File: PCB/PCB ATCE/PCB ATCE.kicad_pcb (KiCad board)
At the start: 2 copper layers, 27 parts, among them J1 USB_OTG, J2 Conn_Coaxial, SW1 SW_Push, SW2 SW_Push, Y1 16MHz

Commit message: PCB
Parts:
- added REF**: MountingHole_3.2mm_M3, MountingHole:MountingHole_3.2mm_M3, F.Cu at (114.5, 106.5)
- added REF**: MountingHole_3.2mm_M3, MountingHole:MountingHole_3.2mm_M3, F.Cu at (158.5, 79.5)
- added TP1: TestPoint, TestPoint:TestPoint_Keystone_5000-5004_Miniature, F.Cu at (138.5, 79.8)
- moved J2 46.6 mm to (154.5, 90.0), turned to 180 degrees
- moved C5 36.6 mm to (126.4, 104.0)
- moved C1 35.4 mm to (143.5, 103.0), turned to 90 degrees
- moved J1 35.2 mm to (118.6, 85.6)
- moved U1 33.3 mm to (138.3, 89.5)
- moved SW1 33.3 mm to (132.5, 101.9), turned to 90 degrees
- moved C7 33.1 mm to (147.5, 93.9), turned to -90 degrees
- moved C2 32.3 mm to (140.0, 103.0), turned to 90 degrees
- moved C3 30.0 mm to (147.5, 103.0), turned to -90 degrees
- moved TP3 28.3 mm to (120.0, 107.0)
- moved TP2 27.8 mm to (129.0, 96.5)
- moved BB833 27.4 mm to (143.5, 106.0), turned to 180 degrees
- moved R1 26.4 mm to (126.5, 92.0), turned to 90 degrees
- moved C6 24.8 mm to (143.5, 81.0), turned to 180 degrees
- moved SW2 24.7 mm to (151.9, 83.5)
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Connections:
- net Net-(J1-D+) renamed /D1+
- net Net-(J1-D-) renamed /D1-
- net Net-(U1-D+) renamed /D2+
- net Net-(U1-D-) renamed /D2-
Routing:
- net +5V: track 0.00 -> 80.0 mm
- net Net-(U2--): track 0.00 -> 34.0 mm
- net GND: track 0.00 -> 32.2 mm, vias 0 -> 23
- net Net-(J1-VBUS): track 0.00 -> 24.1 mm
- net Net-(U2-+): track 0.00 -> 18.4 mm
- net Net-(U1-XTAL2): track 0.00 -> 17.2 mm
- net Net-(U1-(OC0A/OC1C/~{RTS}/PCINT7)PB7): track 0.00 -> 13.7 mm
- net /D2-: track 0.00 -> 13.3 mm
- net Net-(BB833-K): track 0.00 -> 13.2 mm
- net /D2+: track 0.00 -> 12.5 mm
- net Net-(J2-In): track 0.00 -> 11.3 mm
- net Net-(U1-XTAL1): track 0.00 -> 11.0 mm
- net /D1+: track 0.00 -> 9.94 mm
- net /D1-: track 0.00 -> 9.86 mm
- net Net-(U1-(~{HWB})PE2): track 0.00 -> 5.33 mm
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- added copper zone on B.Cu, net GND
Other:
- board outline added: 49 x 32 mm

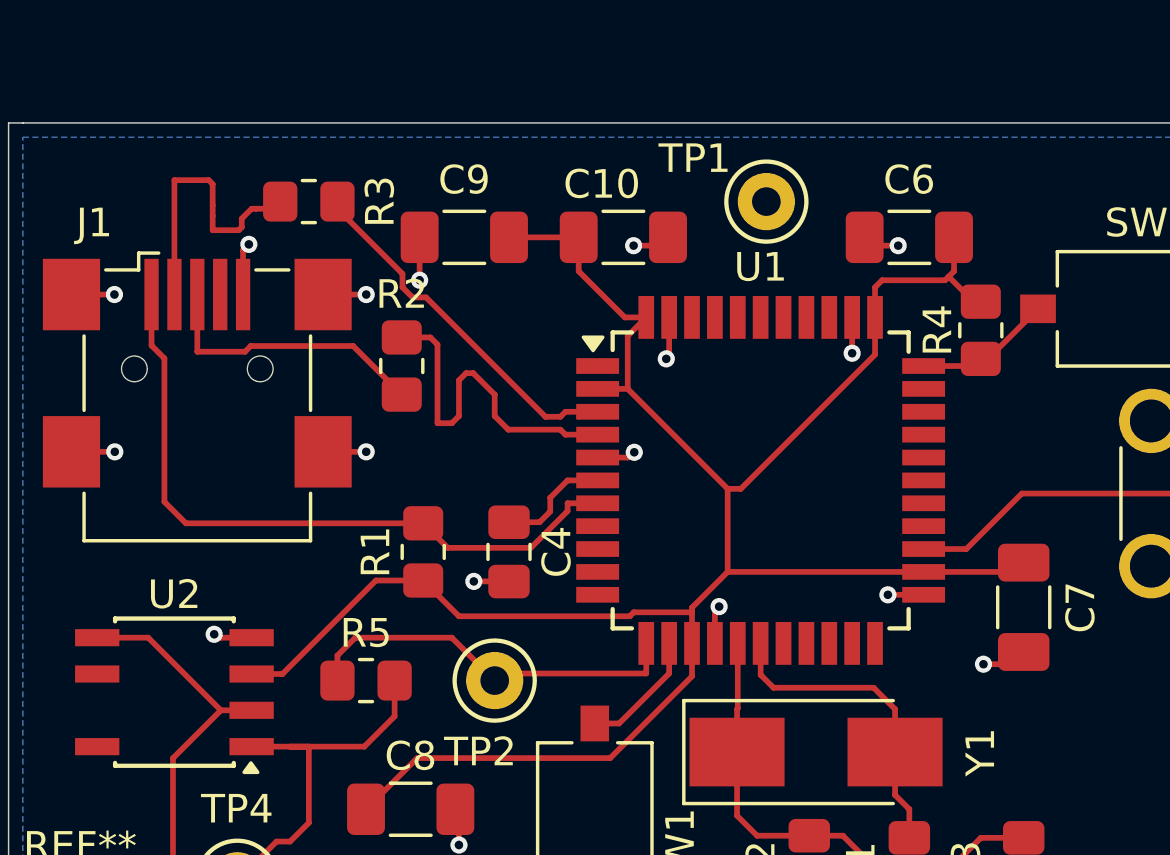
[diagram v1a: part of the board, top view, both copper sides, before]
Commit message: j'ai enlever les 90 degres
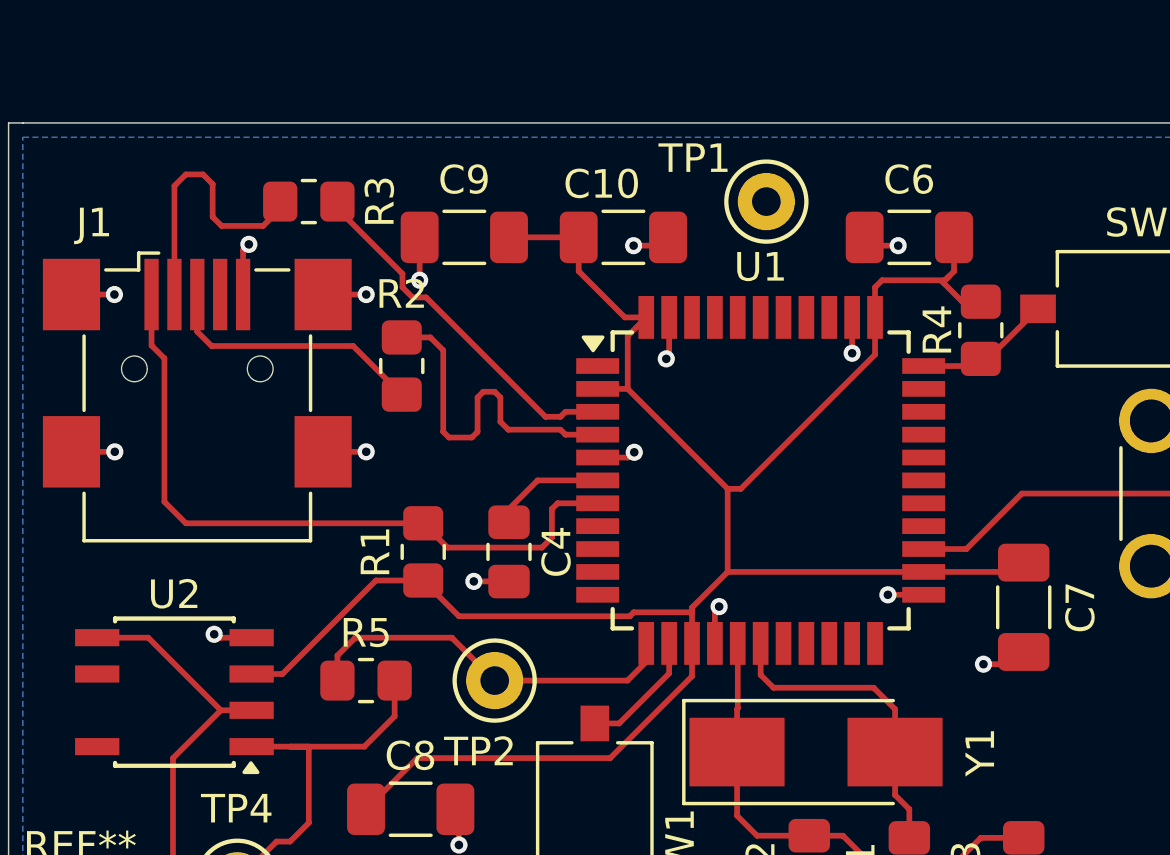
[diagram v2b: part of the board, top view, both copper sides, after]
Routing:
- net /D1+: track 9.94 -> 9.36 mm
- net /D1-: track 9.86 -> 9.33 mm

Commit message: deplace port usb
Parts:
- moved R3 3.60 mm to (125.8, 81.2), turned to -90 degrees
- moved J1 3.60 mm to (118.6, 82.0)
- moved C9 1.31 mm to (129.2, 81.4), turned to -90 degrees
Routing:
- net /D1-: track 9.33 -> 14.8 mm
- net /D1+: track 9.36 -> 14.1 mm
- net Net-(J1-VBUS): track 24.5 -> 27.8 mm
- net /D2-: track 13.3 -> 10.1 mm
- net /D2+: track 12.5 -> 9.28 mm
- net +5V: track 80.4 -> 81.7 mm

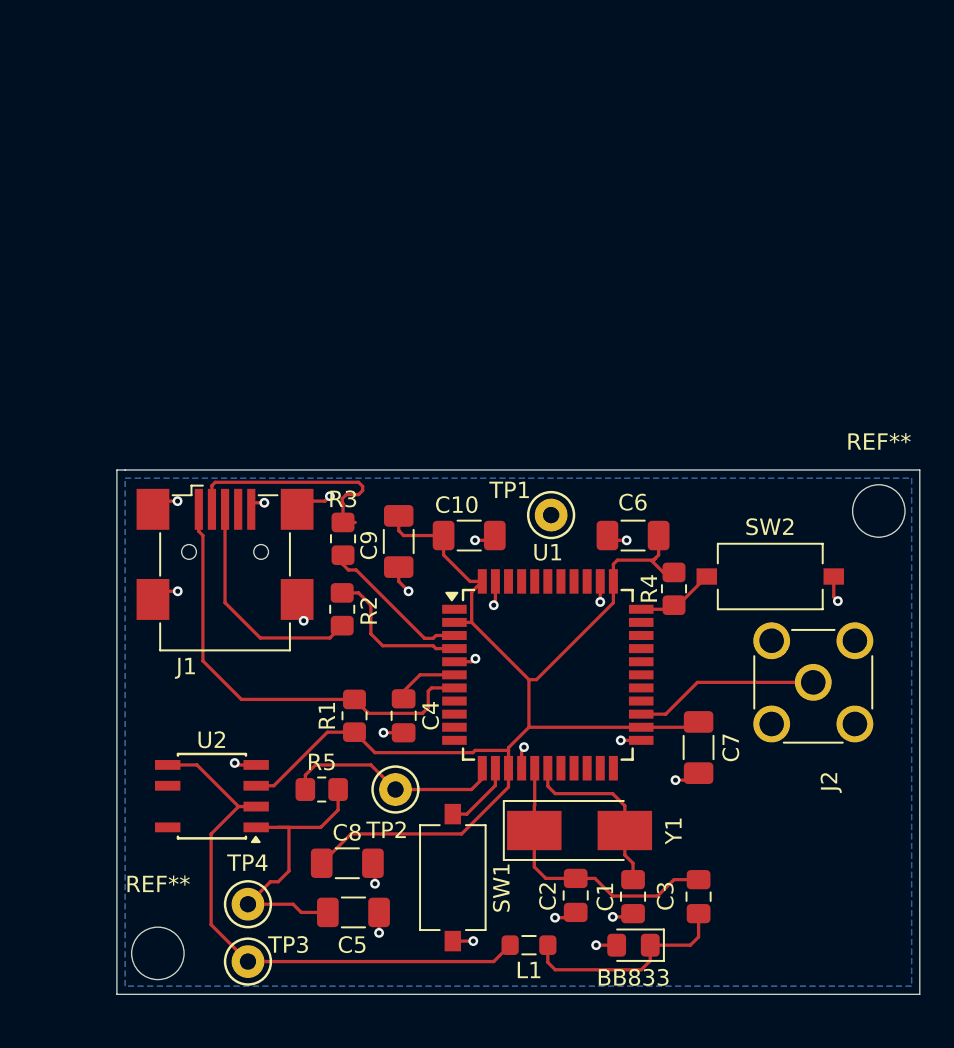
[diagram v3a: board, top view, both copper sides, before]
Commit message: PCB : retouche port usb et coax
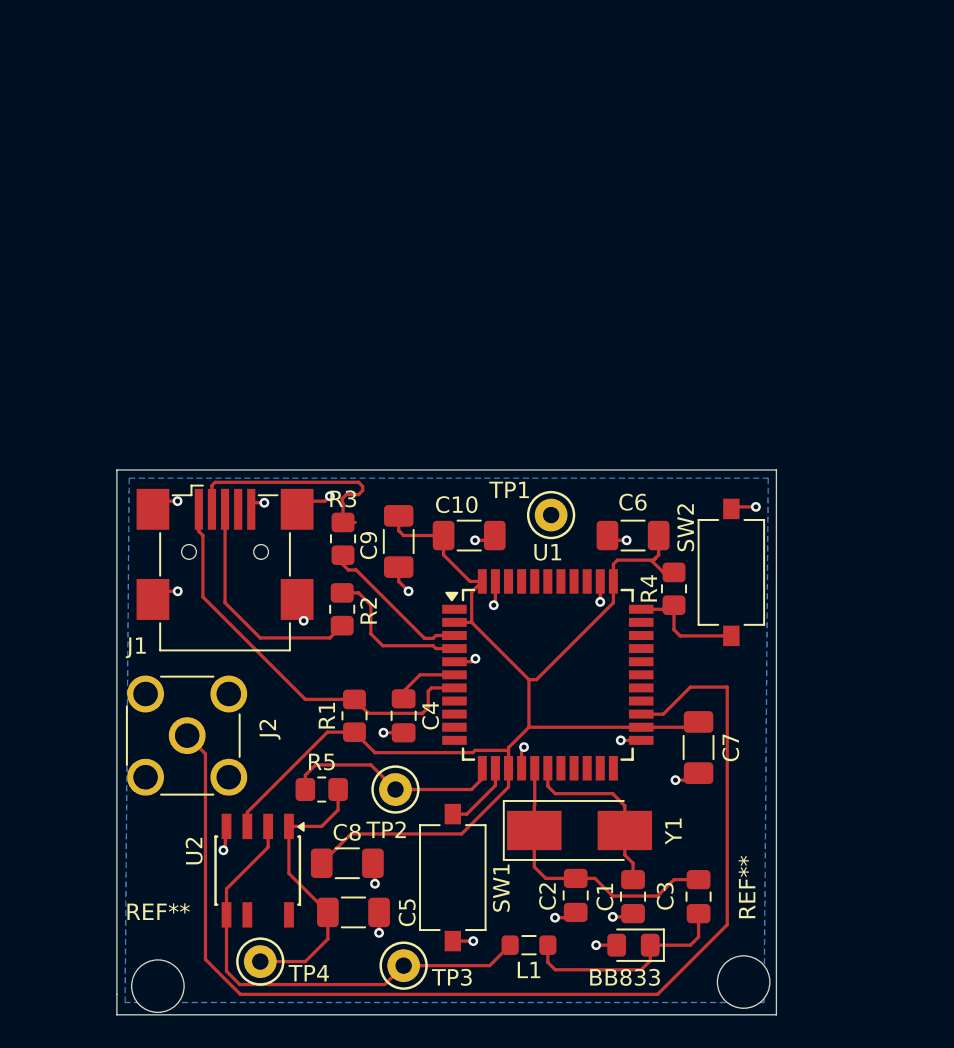
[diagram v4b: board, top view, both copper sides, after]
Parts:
- moved J2 38.3 mm to (116.3, 93.2), turned to 90 degrees
- moved REF** 29.9 mm to (150.2, 108.2), turned to 90 degrees
- moved TP3 9.50 mm to (129.5, 107.2)
- moved U2 5.34 mm to (120.6, 101.5), turned to -90 degrees
- moved TP4 3.58 mm to (120.8, 107.0)
- moved SW2 2.39 mm to (149.5, 83.2), turned to 90 degrees
- moved REF** 2.00 mm to (114.5, 108.5)
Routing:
- net Net-(J2-In): track 11.3 -> 69.0 mm
- net Net-(U2--): track 34.0 -> 28.5 mm
- net Net-(U1-(~{HWB})PE2): track 5.33 -> 8.01 mm
- net Net-(J1-VBUS): track 27.8 -> 25.5 mm
- net +5V: track 81.7 -> 83.8 mm
- net Net-(U2-+): track 18.4 -> 17.7 mm
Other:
- board size 49 x 32 mm -> 40.2 x 33.2 mm

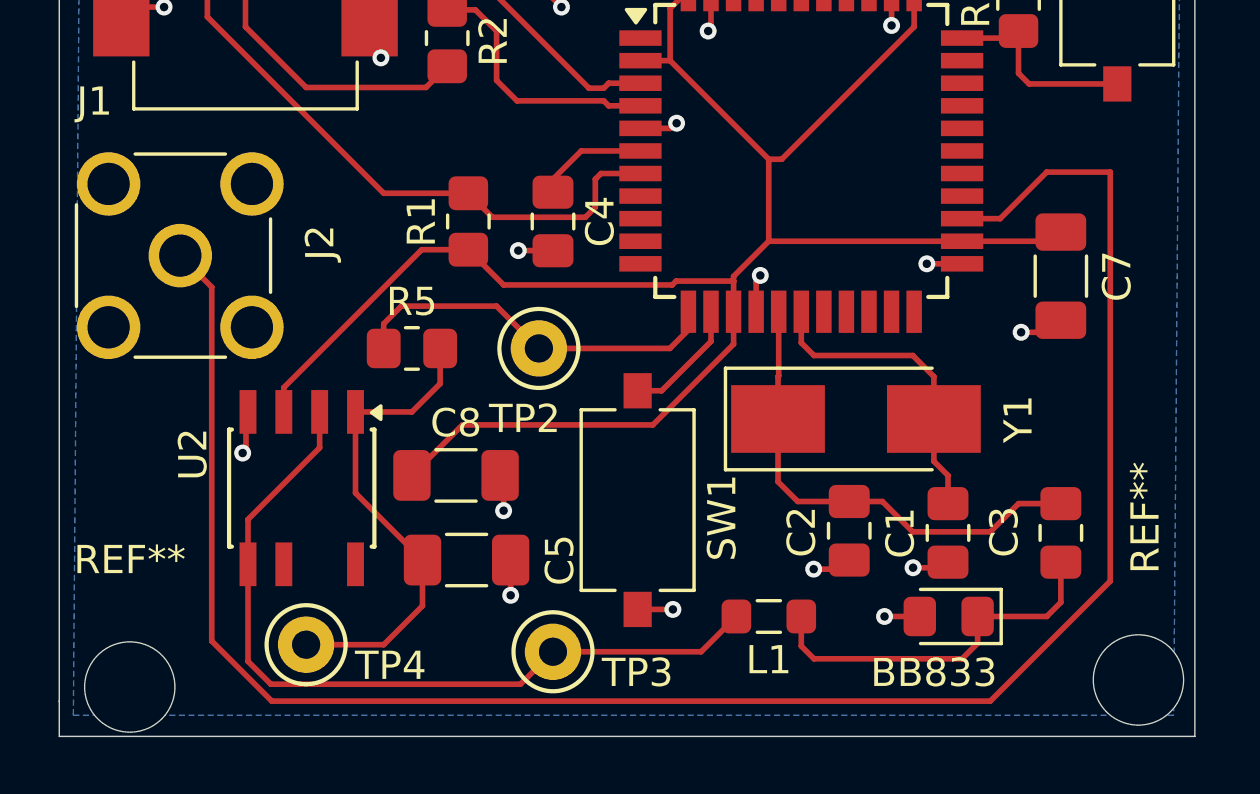
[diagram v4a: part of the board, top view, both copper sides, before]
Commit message: suppression dossier Maxime + Deplacement des trou pcb
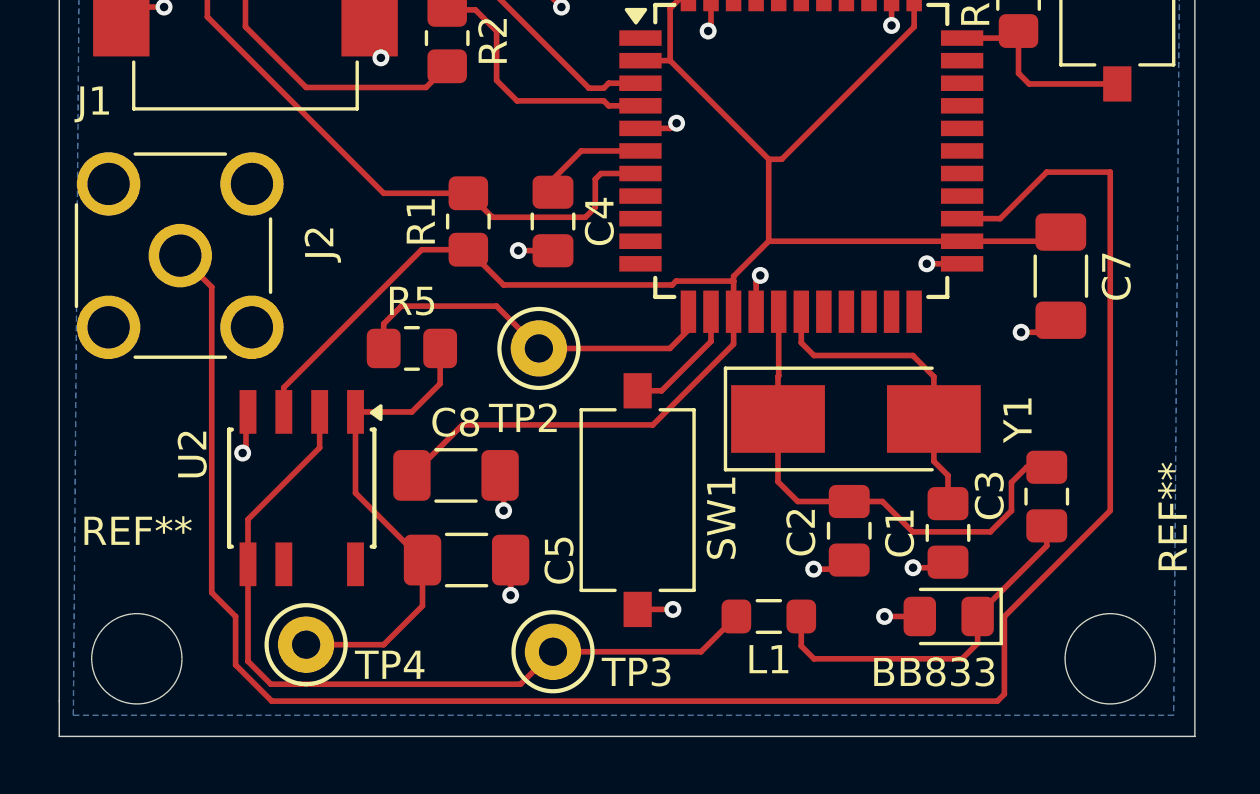
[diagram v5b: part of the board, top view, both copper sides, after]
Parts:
- moved C3 1.38 mm to (147.0, 101.8)
- moved REF** 1.25 mm to (149.2, 107.5)
- moved REF** 1.03 mm to (114.8, 107.5)
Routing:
- net Net-(U1-XTAL2): track 17.2 -> 17.8 mm
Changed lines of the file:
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@@
 		(tags "resistor handsolder")
 		(property "Reference" "R3"
-			(at -2.4 0 360)
+			(at -2.4 0 0)
 			(layer "F.SilkS")
 			(effects
@@
 	(footprint "Capacitor_SMD:C_0805_2012Metric_Pad1.18x1.45mm_HandSolder"
 		(layer "F.Cu")
-		(at 147.5 103.0375 -90)
+		(at 147 101.75 -90)
 		(descr "Capacitor SMD 0805 (2012 Metric), square (rectangular) end terminal, IPC_7351 nominal with elongated pad for handsoldering. (Body size source: IPC-SM-782 page 76, https://www.pcb-3d.com/wordpress/wp-content/uploads/ipc-sm-782a_amendment_1_and_2.pdf, https://docs.google.com/spreadsheets/d/1BsfQQcO9C6DZCsRaXUlFlo91Tg2WpOkGARC1WS5S8t0/edit?usp=sharing), generated with kicad-footprint-generator")
 		(tags "capacitor handsolder")
@@
 	(footprint "MountingHole:MountingHole_3.2mm_M3"
 		(layer "F.Cu")
-		(at 114.5 108.5)
+		(at 114.75 107.5)
 		(descr "Mounting Hole 3.2mm, no annular, M3")
 		(tags "mounting hole 3.2mm no annular m3")
@@
 	(footprint "MountingHole:MountingHole_3.2mm_M3"
 		(layer "F.Cu")
-		(at 150.25 108.25 90)
+		(at 149.25 107.5 90)
 		(descr "Mounting Hole 3.2mm, no annular, M3")
 		(tags "mounting hole 3.2mm no annular m3")
 		(property "Reference" "REF**"
-			(at 5.75 0.25 90)
+			(at 5 2.25 90)
 			(layer "F.SilkS")
 			(effects
@@
 	)
 	(segment
-		(start 147 106)
-		(end 144.55 106)
+		(start 144.55 106)
+		(end 144.55 105.95)
 		(width 0.2)
 		(layer "F.Cu")
@@
 	)
 	(segment
-		(start 144.55 106.95)
-		(end 144.55 106)
+		(start 147 103.5)
+		(end 147 102.7875)
 		(width 0.2)
 		(layer "F.Cu")
@@
 	)
 	(segment
-		(start 144 107.5)
-		(end 144.55 106.95)
+		(start 144.55 106.95)
+		(end 144.55 106)
 		(width 0.2)
 		(layer "F.Cu")
@@
 	)
 	(segment
-		(start 147.5 105.5)
-		(end 147 106)
+		(start 144 107.5)
+		(end 144.55 106.95)
 		(width 0.2)
 		(layer "F.Cu")
@@
 	)
 	(segment
-		(start 147.5 104.075)
-		(end 147.5 105.5)
+		(start 144.55 105.95)
+		(end 147 103.5)
 		(width 0.2)
 		(layer "F.Cu")
@@
 	)
 	(segment
-		(start 146 102)
-		(end 145 103)
-		(width 0.2)
-		(layer "F.Cu")
-		(net 4)
-	)
-	(segment
-		(start 147.5 102)
-		(end 146 102)
+		(start 137.475 99)
+		(end 137.475 97.4983)
 		(width 0.2)
 		(layer "F.Cu")
@@
 	)
 	(segment
-		(start 137.475 99)
-		(end 137.475 97.4983)
+		(start 147 100.7125)
+		(end 146.2875 100.7125)
 		(width 0.2)
 		(layer "F.Cu")
@@
 	)
 	(segment
+		(start 145.75 101.25)
+		(end 145.75 102.25)
+		(width 0.2)
+		(layer "F.Cu")
+		(net 4)
+	)
+	(segment
 		(start 142.25 103)
 		(end 141.175 101.925)
@@
 	)
 	(segment
+		(start 146.2875 100.7125)
+		(end 145.75 101.25)
+		(width 0.2)
+		(layer "F.Cu")
+		(net 4)
+	)
+	(segment
 		(start 137.475 101.225)
 		(end 138.175 101.925)
@@
 	)
 	(segment
+		(start 145.75 102.25)
+		(end 145 103)
+		(width 0.2)
+		(layer "F.Cu")
+		(net 4)
+	)
+	(segment
 		(start 129.5 90.5)
 		(end 129.5 90.9625)
@@
 	)
 	(segment
-		(start 147 90.25)
-		(end 149.25 90.25)
+		(start 145.25 109)
+		(end 145.5 108.75)
 		(width 0.2)
 		(layer "F.Cu")
@@
 	)
 	(segment
-		(start 149.25 104.75)
-		(end 145 109)
+		(start 149.25 102.25)
+		(end 149.25 90.25)
 		(width 0.2)
 		(layer "F.Cu")
@@
 	)
 	(segment
-		(start 149.25 90.25)
-		(end 149.25 104.75)
+		(start 145.5 108.75)
+		(end 145.5 106)
 		(width 0.2)
 		(layer "F.Cu")
@@
 	)
 	(segment
-		(start 145 109)
-		(end 119.534314 109)
+		(start 118.25 106)
+		(end 118.25 107.715686)
 		(width 0.2)
 		(layer "F.Cu")
@@
 	)
 	(segment
-		(start 117.405 106.870686)
+		(start 116.29 93.21)
 		(end 117.405 94.325)
 		(width 0.2)
@@
 	(segment
 		(start 145.35 91.9)
-		(end 147 90.25)
+		(end 144 91.9)
 		(width 0.2)
 		(layer "F.Cu")
@@
 	)
 	(segment
-		(start 117.405 94.325)
-		(end 116.29 93.21)
+		(start 117.405 105.155)
+		(end 118.25 106)
 		(width 0.2)
 		(layer "F.Cu")
@@
 	(segment
 		(start 119.534314 109)
-		(end 117.405 106.870686)
+		(end 145.25 109)
 		(width 0.2)
 		(layer "F.Cu")
@@
 	)
 	(segment
-		(start 144 91.9)
+		(start 118.25 107.715686)
+		(end 119.534314 109)
+		(width 0.2)
+		(layer "F.Cu")
+		(net 10)
+	)
+	(segment
+		(start 147 90.25)
 		(end 145.35 91.9)
 		(width 0.2)
 		(layer "F.Cu")
+		(net 10)
+	)
+	(segment
+		(start 145.5 106)
+		(end 149.25 102.25)
+		(width 0.2)
+		(layer "F.Cu")
+		(net 10)
+	)
+	(segment
+		(start 117.405 94.325)
+		(end 117.405 105.155)
+		(width 0.2)
+		(layer "F.Cu")
+		(net 10)
+	)
+	(segment
+		(start 149.25 90.25)
+		(end 147 90.25)
+		(width 0.2)
+		(layer "F.Cu")
